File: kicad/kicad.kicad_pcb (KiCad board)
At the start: 2 copper layers, 102 x 102 mm, 72 parts

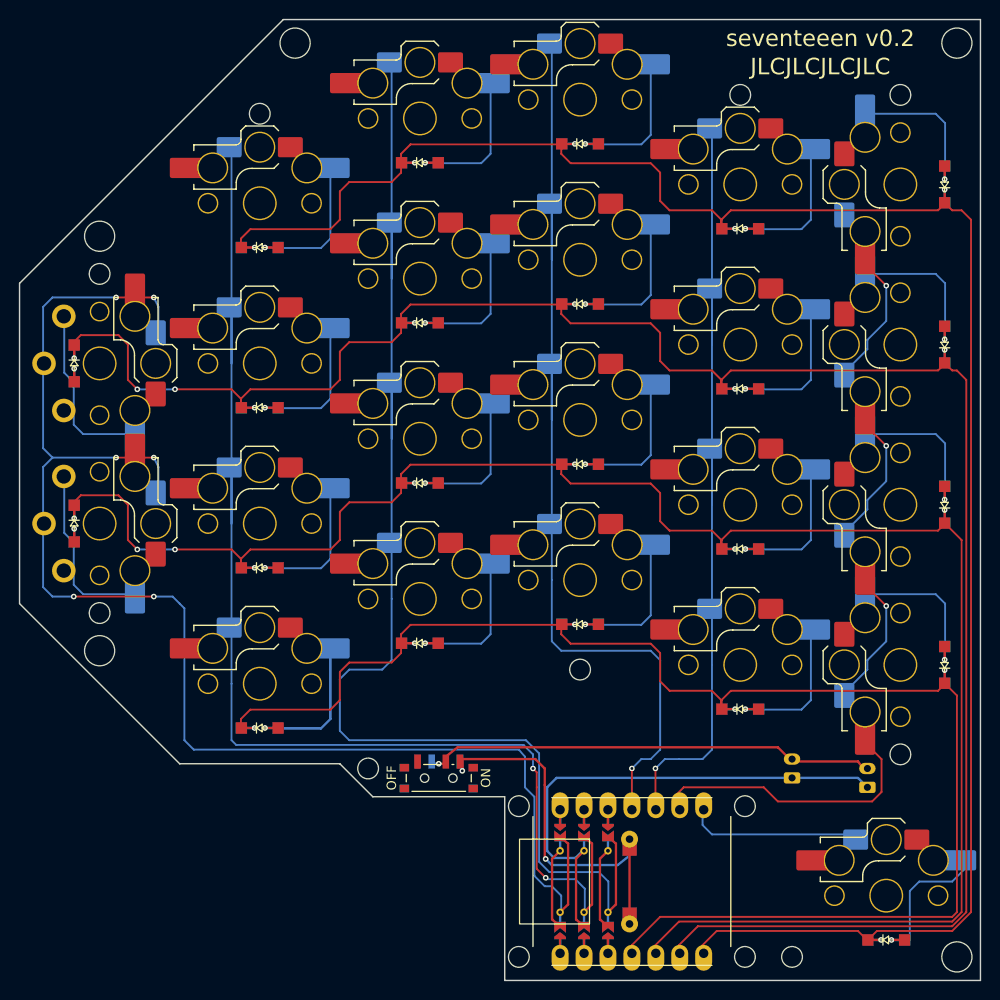
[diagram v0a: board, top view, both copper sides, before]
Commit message: kicad: make a blank version for experimenting
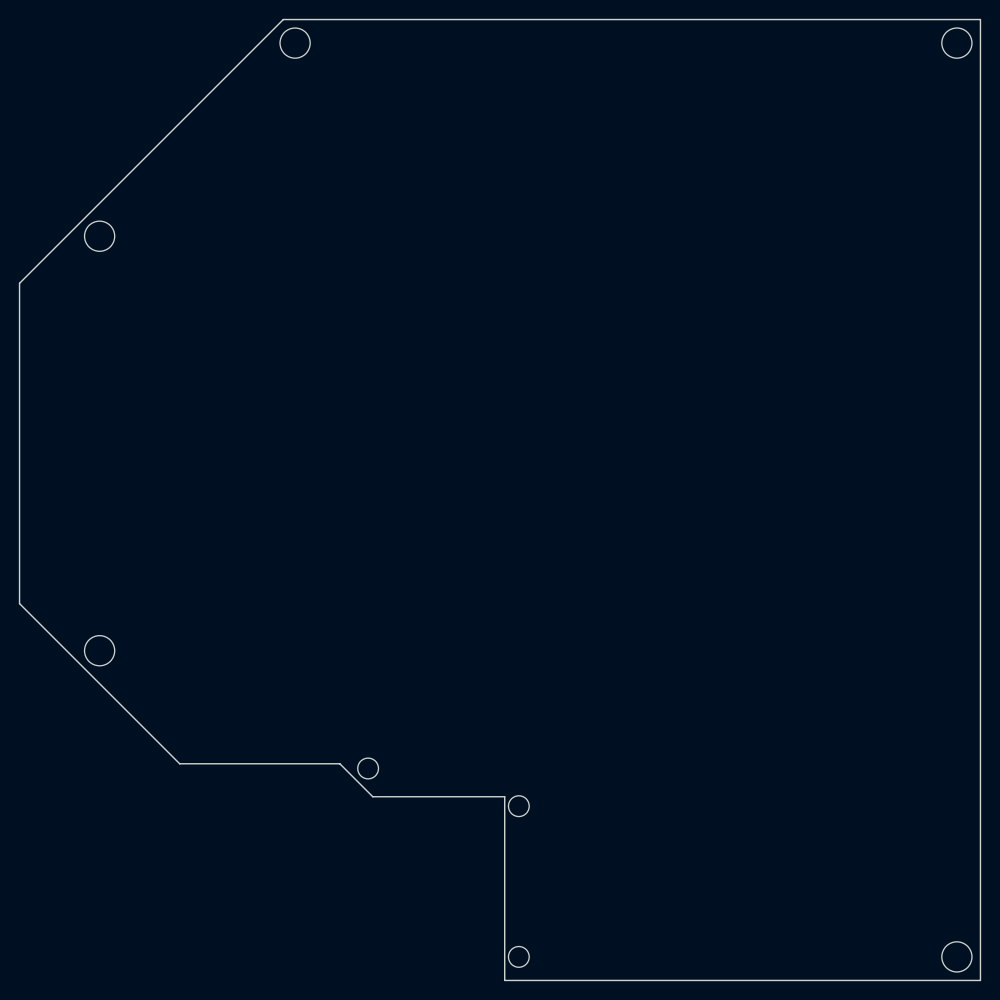
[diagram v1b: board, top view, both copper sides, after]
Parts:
- removed ?: , xiao-ble-tht
- removed D1, D10, D11, D12, D13, D14, D15, D16, D17, D18, D19, D2, D20, D21, D22, D23, D3, D4, D5, D6, D7, D8, D9: , ceoloide:diode_tht_sod123
- removed H1, H2: , ceoloide:mounting_hole_plated
- removed JST1, JST2: , ceoloide:battery_connector_jst_ph_2
- removed MH1, MH10, MH11, MH12, MH2, MH5, MH6, MH7, MH8, MH9: , ceoloide:mounting_hole_npth
- removed PAD1, PAD2: , SMDPad
- removed PWR1: , ceoloide:power_switch_smd_side
- removed S1, S10, S11, S12, S13, S14, S15, S16, S17, S18, S19, S2, S20, S21, S22, S23, S3, S4, S5, S6, S7, S8, S9: , ceoloide:switch_choc_v1_v2
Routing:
- net P5: track 221.9 -> 0.00 mm, vias 8 -> 0
- net P6: track 213.6 -> 0.00 mm, vias 6 -> 0
- net P4: track 206.2 -> 0.00 mm, vias 8 -> 0
- net P3: track 164.4 -> 0.00 mm, vias 5 -> 0
- net P0: track 157.5 -> 0.00 mm, vias 6 -> 0
- net P2: track 142.7 -> 0.00 mm
- net P1: track 138.7 -> 0.00 mm, vias 2 -> 0
- net P10: track 105.7 -> 0.00 mm, vias 1 -> 0
- net P9: track 89.3 -> 0.00 mm, vias 1 -> 0
- net P8: track 67.5 -> 0.00 mm, vias 3 -> 0
- net GND: track 56.6 -> 0.00 mm
- net BAT_P: track 48.2 -> 0.00 mm, vias 1 -> 0
- net BAT_PS: track 39.8 -> 0.00 mm, vias 2 -> 0
- net pinky_bottom: track 26.5 -> 0.00 mm, vias 1 -> 0
- net outer_home: track 21.3 -> 0.00 mm, vias 1 -> 0
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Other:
- board text removed: "JLCJLCJLCJLC"
- board text removed: "seventeeen v0.2"
